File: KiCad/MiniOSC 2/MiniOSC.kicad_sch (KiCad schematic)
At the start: 63 parts, among them J1 IDC_BUS, J2 FM_IN, J3 V_OCT_IN, J4 PWM_CV, J5 PULSE_OUT, J6 SAW_OUT, J7 TRI_OUT, Q1 BC558, Q2 BC548, U1 40106, U2 TL074, U3 TL074, U4 TL074

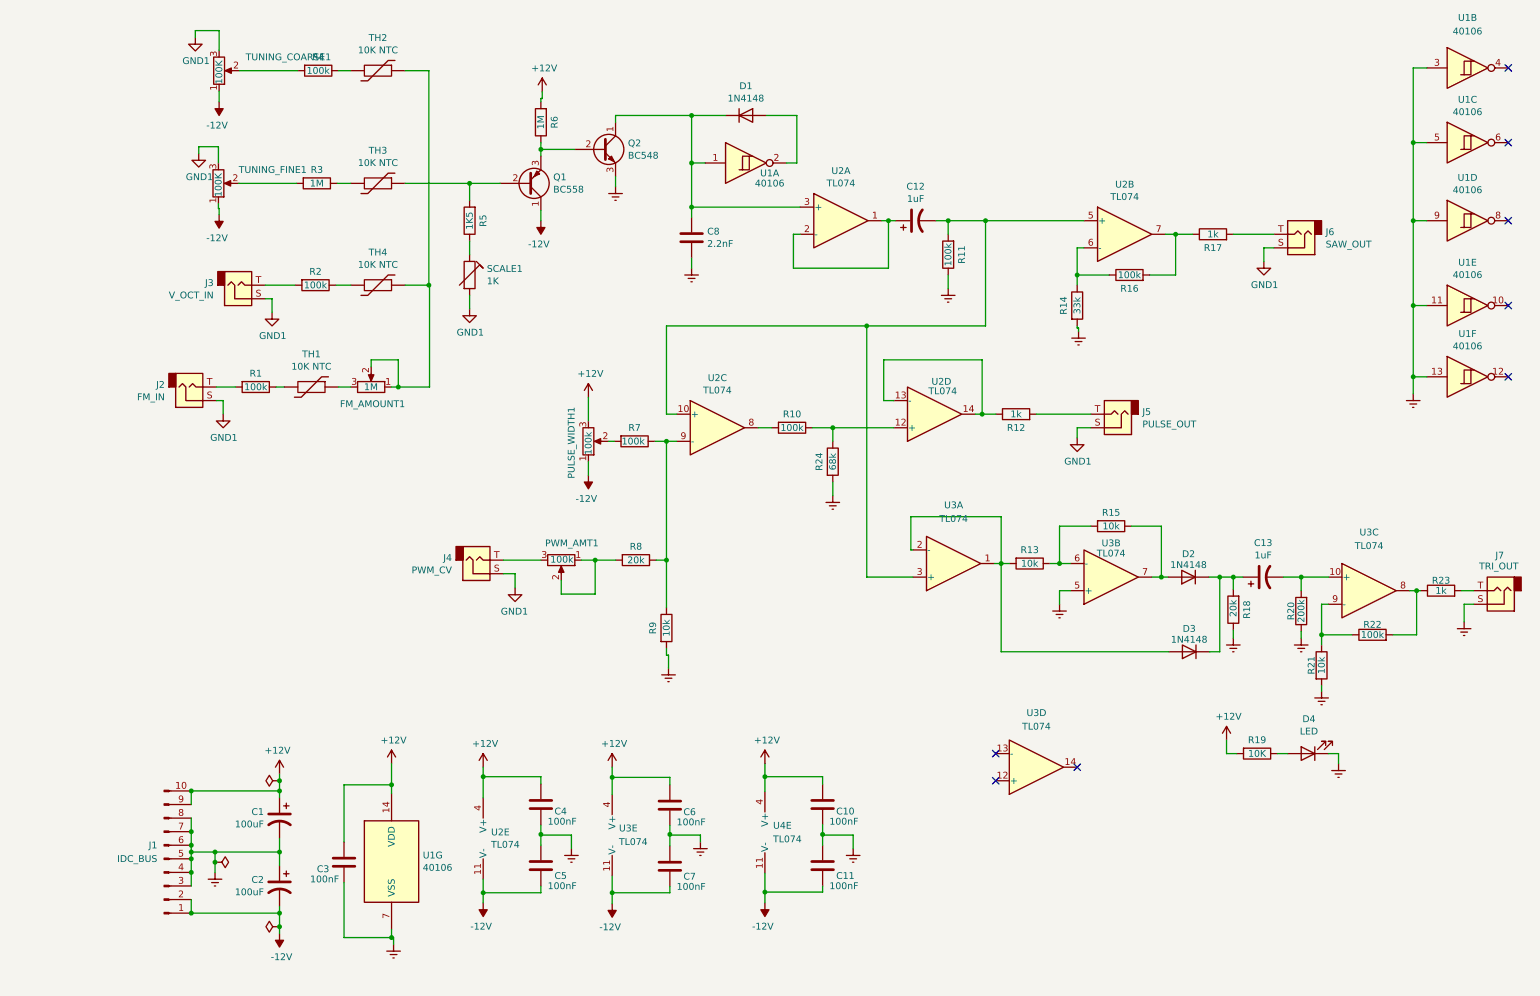
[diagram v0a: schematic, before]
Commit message: updated symbols and grid to kicad 8
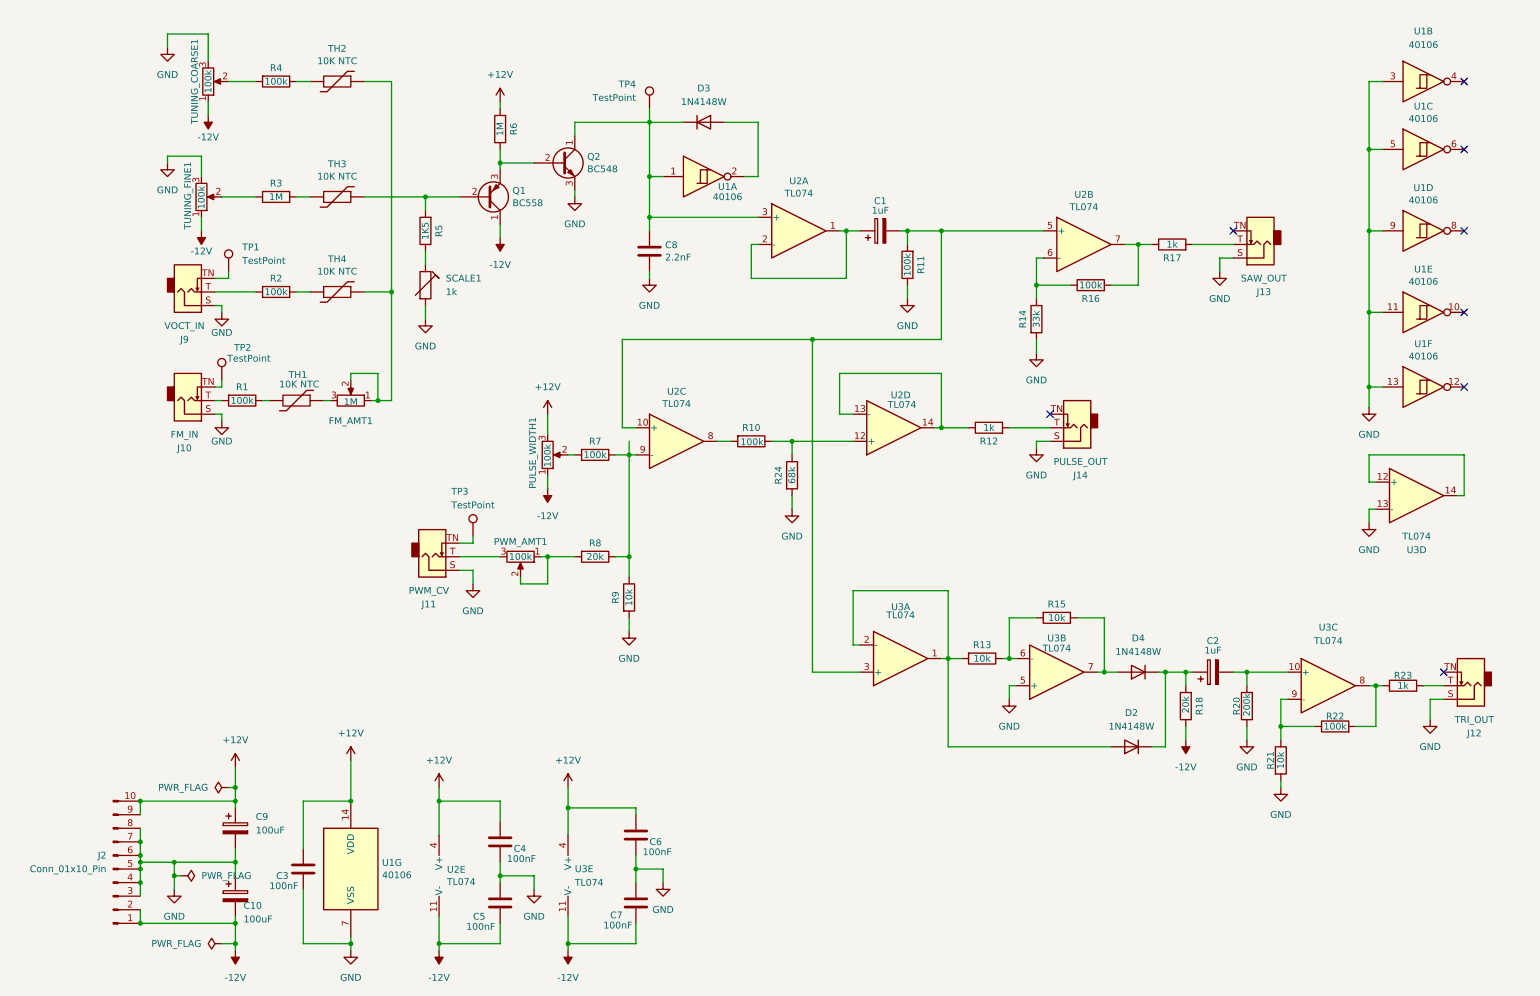
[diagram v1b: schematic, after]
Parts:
- removed C1, C2: 100uF, Capacitor_SMD:C_0805_2012Metric_Pad1.18x1.45mm_HandSolder, symbol MiniOSC-rescue:CP1-Device
- removed C10, C11: 100nF, Capacitor_SMD:C_0603_1608Metric_Pad1.08x0.95mm_HandSolder, symbol Device:C
- removed C12, C13: 1uF, Capacitor_SMD:C_0603_1608Metric_Pad1.08x0.95mm_HandSolder, symbol MiniOSC-rescue:CP1-Device
- removed D1, D2, D3: 1N4148, Diode_SMD:D_SOD-323, symbol Diode:1N4148
- removed D4: LED, LED_THT:LED_D3.0mm, symbol Device:LED
- removed FM_AMOUNT1: 1M, Potentiometer_THT:Potentiometer_Alpha_RD901F-40-00D_Single_Vertical, symbol MiniOSC-rescue:R_POT-Device
- removed J1: IDC_BUS, Connector_IDC:IDC-Header_2x05_P2.54mm_Vertical, symbol Connector:Conn_01x10_Male
- removed J2: FM_IN, Connector_Audio:Jack_3.5mm_QingPu_WQP-PJ398SM_Vertical_CircularHoles, symbol Connector:AudioJack2
- removed J3: V_OCT_IN, Connector_Audio:Jack_3.5mm_QingPu_WQP-PJ398SM_Vertical_CircularHoles, symbol Connector:AudioJack2
- removed J4: PWM_CV, Connector_Audio:Jack_3.5mm_QingPu_WQP-PJ398SM_Vertical_CircularHoles, symbol Connector:AudioJack2
- removed J5: PULSE_OUT, Connector_Audio:Jack_3.5mm_QingPu_WQP-PJ398SM_Vertical_CircularHoles, symbol Connector:AudioJack2
- removed J6: SAW_OUT, Connector_Audio:Jack_3.5mm_QingPu_WQP-PJ398SM_Vertical_CircularHoles, symbol Connector:AudioJack2
- removed J7: TRI_OUT, Connector_Audio:Jack_3.5mm_QingPu_WQP-PJ398SM_Vertical_CircularHoles, symbol Connector:AudioJack2
- removed PULSE_WIDTH1, PWM_AMT1: 100k, Potentiometer_THT:Potentiometer_Alpha_RD901F-40-00D_Single_Vertical, symbol MiniOSC-rescue:R_POT-Device
- removed R19: 10K, Resistor_SMD:R_0603_1608Metric_Pad0.98x0.95mm_HandSolder, symbol Device:R
- removed SCALE1: 1K, Potentiometer_THT:Potentiometer_Bourns_3266Y_Vertical, symbol MiniOSC-rescue:RTRIM-Device
- removed TUNING_COARSE1, TUNING_FINE1: 100K, Potentiometer_THT:Potentiometer_Alpha_RD901F-40-00D_Single_Vertical, symbol MiniOSC-rescue:R_POT-Device
- removed U4: TL074, symbol Amplifier_Operational:TL074
- added C1, C2: 1uF, symbol Device:C_Polarized
- added C10, C9: 100uF, symbol Device:C_Polarized
- added D2, D3, D4: 1N4148W, Diode_SMD:D_SOD-123, symbol Diode:1N4148W
- added FM_AMT1: 1M, symbol Device:R_Potentiometer
- added J10: FM_IN, symbol benjiaomodular:PJ3001F
- added J11: PWM_CV, symbol benjiaomodular:PJ3001F
- added J12: TRI_OUT, symbol benjiaomodular:PJ3001F
- added J13: SAW_OUT, symbol benjiaomodular:PJ3001F
- added J14: PULSE_OUT, symbol benjiaomodular:PJ3001F
- added J2: Conn_01x10_Pin, symbol Connector:Conn_01x10_Pin
- added J9: VOCT_IN, symbol benjiaomodular:PJ3001F
- added PULSE_WIDTH1, PWM_AMT1, TUNING_COARSE1, TUNING_FINE1: 100k, symbol Device:R_Potentiometer
- added SCALE1: 1k, symbol Device:R_Trim
- added TP1, TP2, TP3, TP4: TestPoint, symbol Connector:TestPoint
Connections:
- net +12V: now also C9.1, J2.10 (Pin_10), J2.9 (Pin_9), PULSE_WIDTH1.3
- net -12V: now also R18.1, C10.2, J2.1 (Pin_1), J2.2 (Pin_2), PULSE_WIDTH1.1, TUNING_COARSE1.1, TUNING_FINE1.1
- net at R4.2: now also TUNING_COARSE1.2
- net at R3.2: now also TUNING_FINE1.2
- net at R2.2: now also J9.T
- net at R1.2: now also J10.T
- net at TH1.1: now also FM_AMT1.3
- net at TH2.1, TH4.1: now also FM_AMT1.1, FM_AMT1.2
- net at R5.1: now also SCALE1.1
- net at C8.1, Q2.1 (C), U1.1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: now also D3.1 (K), TP4.1
- net at U1.2: now also D3.2 (A)
- net at U2.1, U2.2 (-): now also C1.1
- net at R11.2, U2.10 (+), U2.5 (+)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: now also C1.2
- net at R17.2: now also J13.T
- net at R12.2: now also J14.T
- net at R20.2, U3.10 (+): now also C2.2
- net at R15.1, U3.7: now also D4.2 (A)
- net at R7.2: now also PULSE_WIDTH1.2
- net at R8.2: now also PWM_AMT1.1, PWM_AMT1.2
- net at U3.12 (+): now also U3.14
- net GND: now reaches U3.13 (-)
- net GND: now also C3.2, C4.2, C5.1, C6.2, C7.1, C8.2, Q2.3 (E), R11.1, R14.2, R20.1, R21.2, R24.2, R9.2, U1.11, U1.13, U1.3, U1.5, U1.7 (VSS), U1.9, U3.5 (+), C10.1, C9.2, J10.S, J11.S, J12.S, J13.S, J14.S, J2.3 (Pin_3), J2.4 (Pin_4), J2.5 (Pin_5), J2.6 (Pin_6), J2.7 (Pin_7), J2.8 (Pin_8), J9.S, SCALE1.2, TUNING_COARSE1.3, TUNING_FINE1.3
- net at R13.2, U3.1, U3.2 (-): now also D2.2 (A)
- net at R18.2: now also C2.1, D2.1 (K), D4.1 (K)
- net at R23.2: now also J12.T
- removed net Earth: C3.2, C4.2, C5.1, C6.2, C7.1, C8.2, Q2.3 (E), R11.1, R14.2, R18.1, R20.1, R21.2, R24.2, R9.2, U1.11, U1.13, U1.3, U1.5, U1.7 (VSS), U1.9, U3.5 (+)
- new net: J10.TN, TP2.1
- new net: J11.TN, TP3.1
- new net: J9.TN, TP1.1
- new net: J11.T, PWM_AMT1.3
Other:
- moved on the sheet: C3, C4, C5, C6, C7, C8, Q1, Q2, R1, R10, R11, R12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
